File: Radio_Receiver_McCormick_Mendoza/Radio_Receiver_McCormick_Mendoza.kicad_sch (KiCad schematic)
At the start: 7 parts

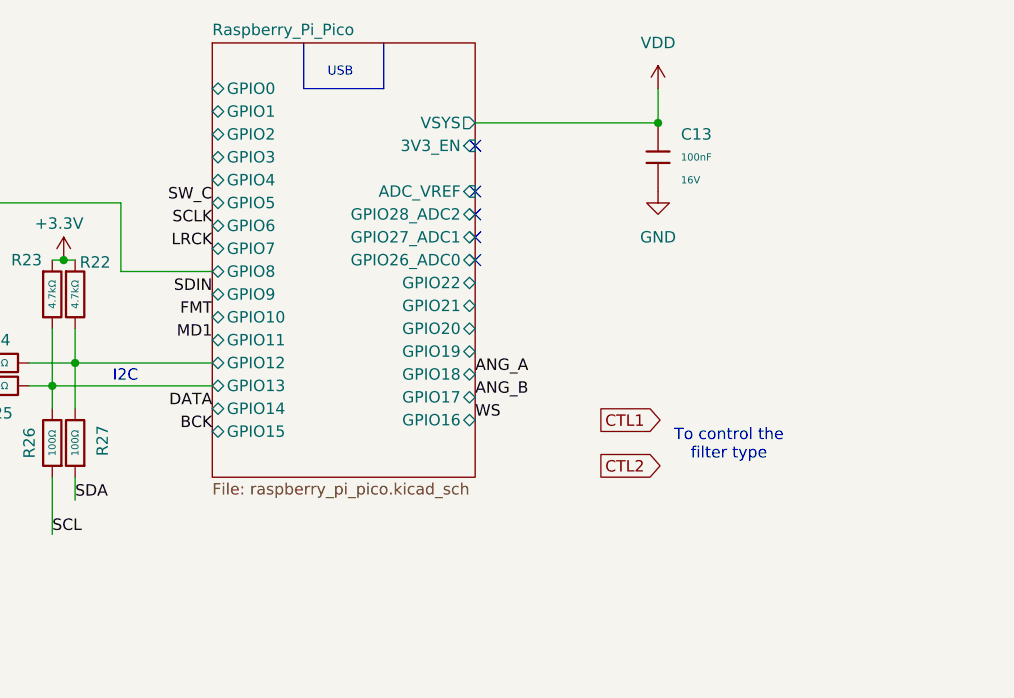
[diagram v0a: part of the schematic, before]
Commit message: Integrated signal path modules
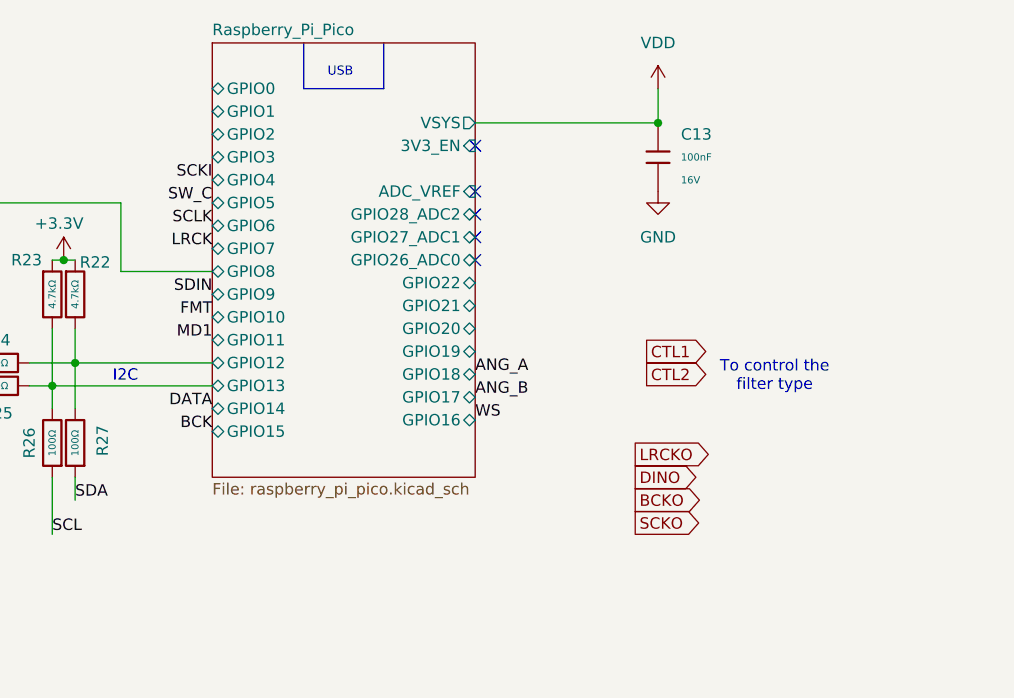
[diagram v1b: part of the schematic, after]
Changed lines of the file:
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@@
 	(text "To control the\nfilter type"
 		(exclude_from_sim no)
-		(at 128.524 80.264 0)
+		(at 133.604 72.644 0)
 		(effects
 			(font
@@
 		)
 	)
+	(label "SCKI"
+		(at 71.12 50.8 180)
+		(effects
+			(font
+				(size 1.27 1.27)
+			)
+			(justify right bottom)
+		)
+	)
 	(label "OSC_SCL"
 		(at 39.37 73.66 180)
@@
 	(global_label "CTL1"
 		(shape output)
-		(at 114.3 77.47 0)
+		(at 119.38 69.85 0)
+		(fields_autoplaced yes)
+		(effects
+			(font
+				(size 1.27 1.27)
+			)
+			(justify left)
+		)
+		(property "Intersheetrefs" "${INTERSHEET_REFS}"
+			(at 126.8404 69.85 0)
+			(hide yes)
+			(show_name no)
+			(do_not_autoplace no)
+			(effects
+				(font
+					(size 1.27 1.27)
+				)
+				(justify left)
+			)
+		)
+	)
+	(global_label "SCKO"
+		(shape output)
+		(at 118.11 88.9 0)
 		(fields_autoplaced yes)
 		(effects
@@
 		)
 		(property "Intersheetrefs" "${INTERSHEET_REFS}"
-			(at 121.7604 77.47 0)
+			(at 126.1752 88.9 0)
+			(hide yes)
+			(show_name no)
+			(do_not_autoplace no)
+			(effects
+				(font
+					(size 1.27 1.27)
+				)
+				(justify left)
+			)
+		)
+	)
+	(global_label "LRCKO"
+		(shape output)
+		(at 118.11 81.28 0)
+		(fields_autoplaced yes)
+		(effects
+			(font
+				(size 1.27 1.27)
+			)
+			(justify left)
+		)
+		(property "Intersheetrefs" "${INTERSHEET_REFS}"
+			(at 127.2638 81.28 0)
+			(hide yes)
+			(show_name no)
+			(do_not_autoplace no)
+			(effects
+				(font
+					(size 1.27 1.27)
+				)
+				(justify left)
+			)
+		)
+	)
+	(global_label "DINO"
+		(shape output)
+		(at 118.11 83.82 0)
+		(fields_autoplaced yes)
+		(effects
+			(font
+				(size 1.27 1.27)
+			)
+			(justify left)
+		)
+		(property "Intersheetrefs" "${INTERSHEET_REFS}"
+			(at 125.631 83.82 0)
 			(hide yes)
 			(show_name no)
@@
 	(global_label "CTL2"
 		(shape output)
-		(at 114.3 82.55 0)
+		(at 119.38 72.39 0)
+		(fields_autoplaced yes)
+		(effects
+			(font
+				(size 1.27 1.27)
+			)
+			(justify left)
+		)
+		(property "Intersheetrefs" "${INTERSHEET_REFS}"
+			(at 126.8404 72.39 0)
+			(hide yes)
+			(show_name no)
+			(do_not_autoplace no)
+			(effects
+				(font
+					(size 1.27 1.27)
+				)
+				(justify left)
+			)
+		)
+	)
+	(global_label "BCKO"
+		(shape output)
+		(at 118.11 86.36 0)
 		(fields_autoplaced yes)
 		(effects
@@
 		)
 		(property "Intersheetrefs" "${INTERSHEET_REFS}"
-			(at 121.7604 82.55 0)
+			(at 126.2357 86.36 0)
 			(hide yes)
 			(show_name no)

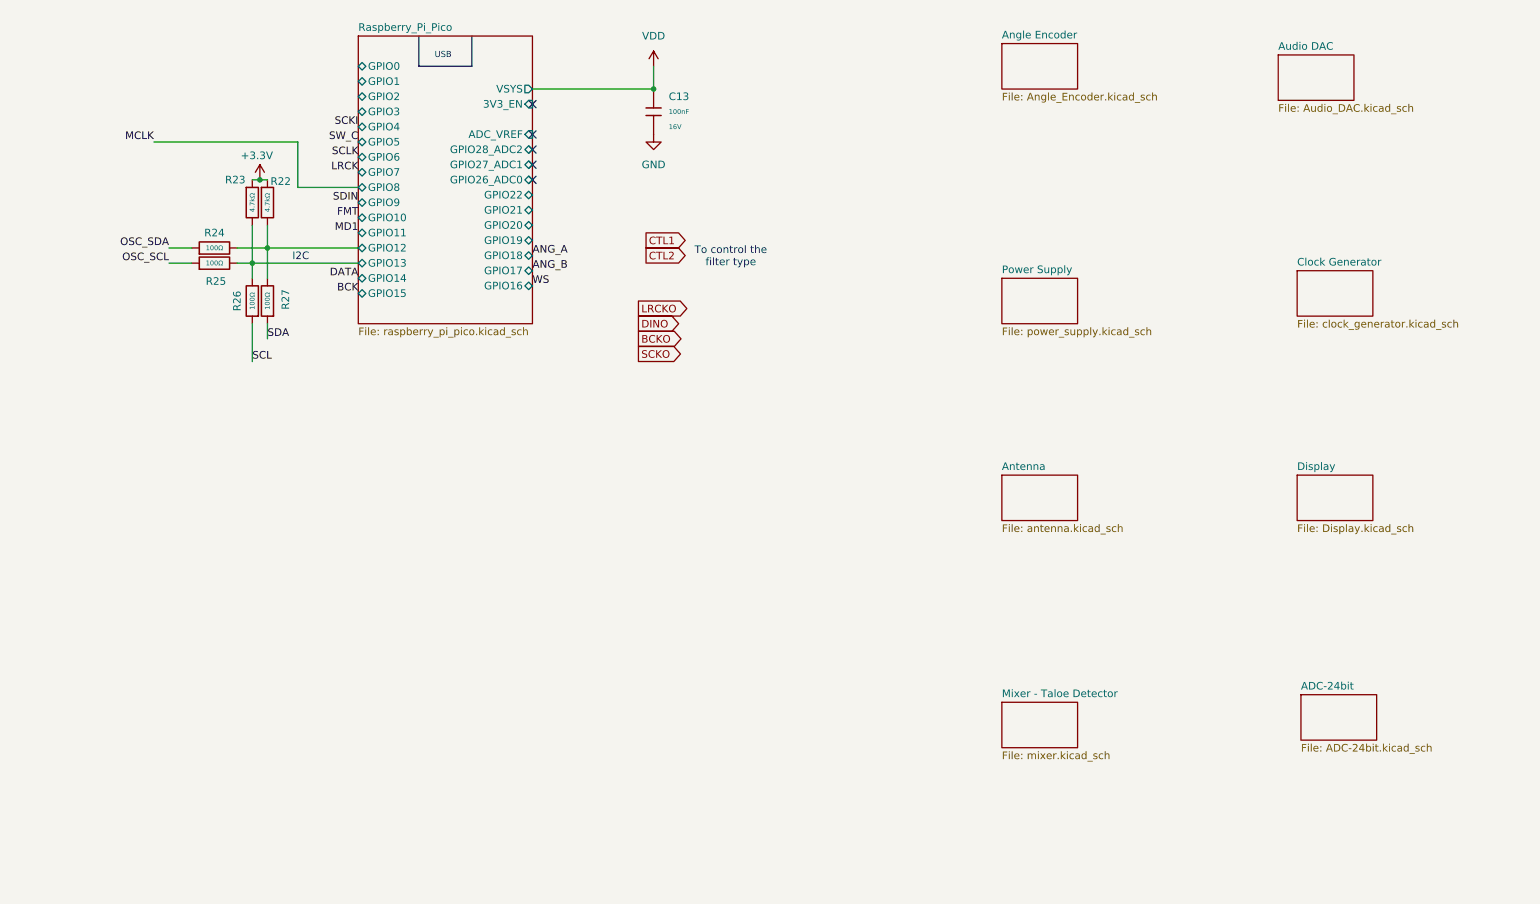
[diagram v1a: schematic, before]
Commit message: Finalized Pico connections and added indicator LEDs
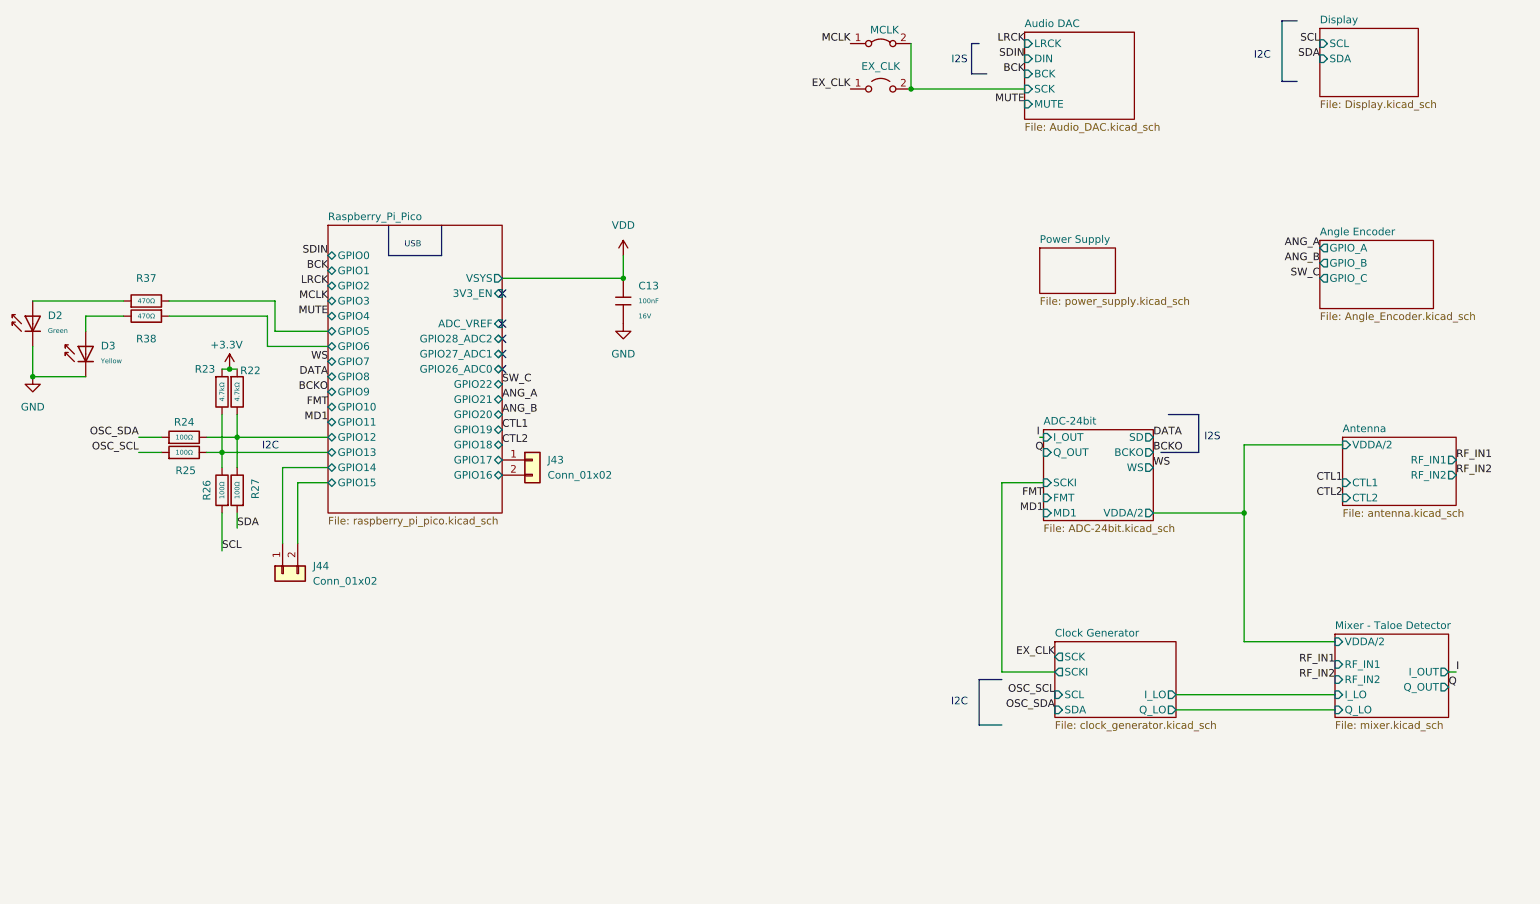
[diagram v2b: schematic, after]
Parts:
- added D2: Green, PCM_JLCPCB:D_0805, symbol PCM_JLCPCB-Diodes:LED,0805,Green
- added D3: Yellow, PCM_JLCPCB:D_0805, symbol PCM_JLCPCB-Diodes:LED,0805,Yellow
- added J43, J44: Conn_01x02, Connector_PinHeader_2.54mm:PinHeader_1x02_P2.54mm_Vertical, symbol Connector_Generic:Conn_01x02
- added JP13: EX_CLK, Jumper:SolderJumper-2_P1.3mm_Open_RoundedPad1.0x1.5mm, symbol Jumper:Jumper_2_Open
- added R37, R38: 470Ω, PCM_JLCPCB:R_0603, symbol PCM_JLCPCB-Resistors:0603,470Ω
- added e9: MCLK, Jumper:SolderJumper-2_P1.3mm_Bridged_RoundedPad1.0x1.5mm, symbol Jumper:Jumper_2_Bridged
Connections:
- net GND: now also D2.1, D3.1
- net MCLK: now also e9.1 (A)
- new net: D2.2, R37.1
- new net: D3.2, R38.2
- new net Audio DAC/SCK: JP13.2 (B), e9.2 (B)
- new net EX_CLK: JP13.1 (A)
- new net Raspberry_Pi_Pico/GPIO14: J44.1 (Pin_1)
- new net Raspberry_Pi_Pico/GPIO15: J44.2 (Pin_2)
- new net Raspberry_Pi_Pico/GPIO16: J43.2 (Pin_2)
- new net Raspberry_Pi_Pico/GPIO17: J43.1 (Pin_1)
- new net Raspberry_Pi_Pico/GPIO5: R37.2
- new net Raspberry_Pi_Pico/GPIO6: R38.1
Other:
- sheet ADC-24bit ports: added BCKO, FMT, I_OUT, MD1, Q_OUT, SCKI, SD, VDDA/2, WS; removed none
- sheet Angle Encoder ports: added GPIO_A, GPIO_B, GPIO_C; removed none
- sheet Antenna ports: added CTL1, CTL2, RF_IN1, RF_IN2, VDDA/2; removed none
- sheet Audio DAC ports: added BCK, DIN, LRCK, MUTE, SCK; removed none
- sheet Clock Generator ports: added I_LO, Q_LO, SCK, SCKI, SCL, SDA; removed none
- sheet Display ports: added SCL, SDA; removed none
- sheet Mixer - Taloe Detector ports: added I_LO, I_OUT, Q_LO, Q_OUT, RF_IN1, RF_IN2, VDDA/2; removed none
- note added: "I2S"
- note removed: "To control the filter type"
- moved on the sheet: C13, R22, R23, R24, R25, R26, R27

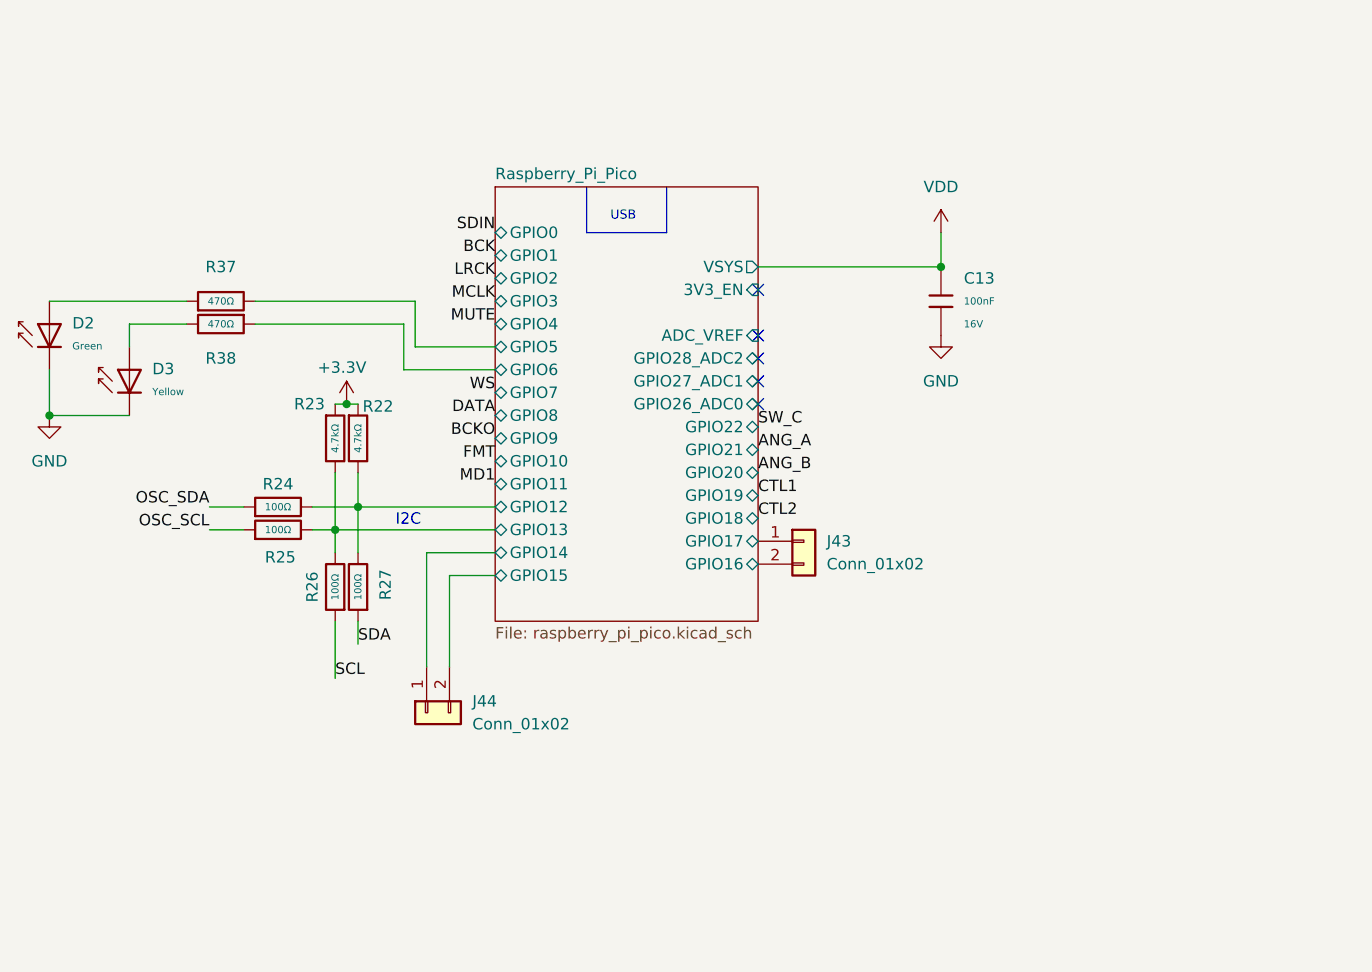
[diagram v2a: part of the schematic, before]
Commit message: Added transformer footprint and datasheet
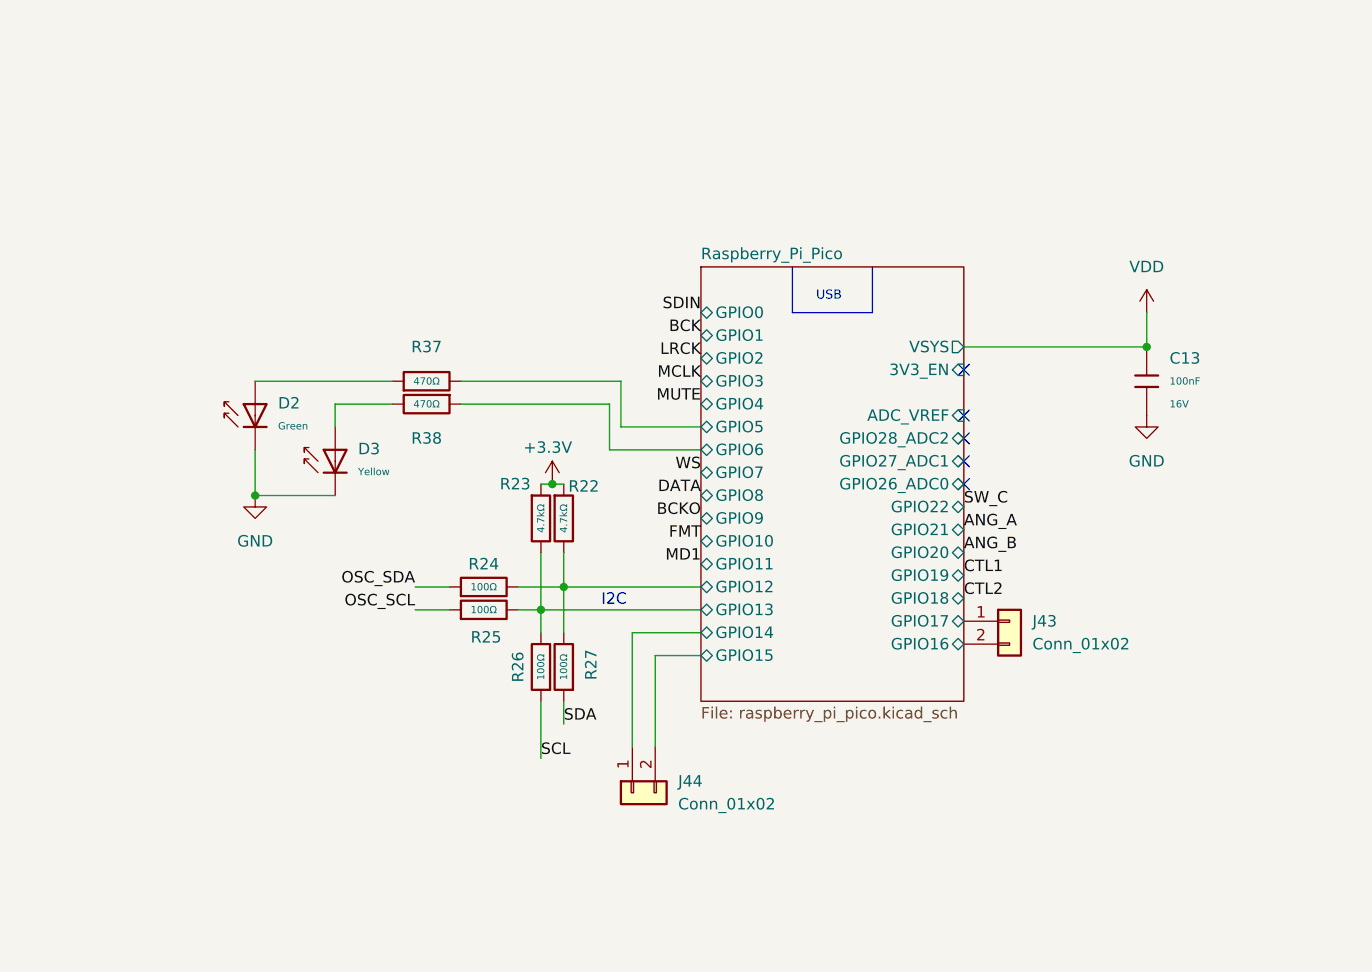
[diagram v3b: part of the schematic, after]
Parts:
- D2, D3: Manufacturer Hubei KENTO Elec -> (none)
- R37, R38: Manufacturer UNI-ROYAL(Uniroyal Elec) -> (none)
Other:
- moved on the sheet: C13, D2, D3, J43, J44, R22, R23, R24, R25, R26, R27, R37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

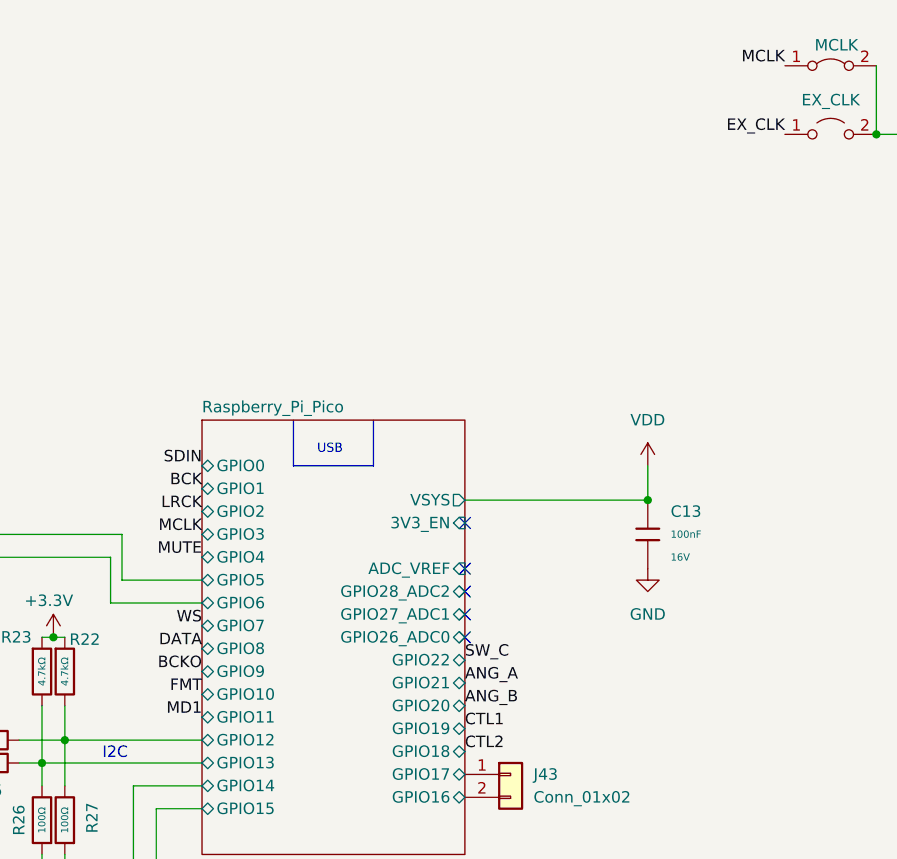
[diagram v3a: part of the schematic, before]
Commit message: Swapped voltage regulator to output 4.5V
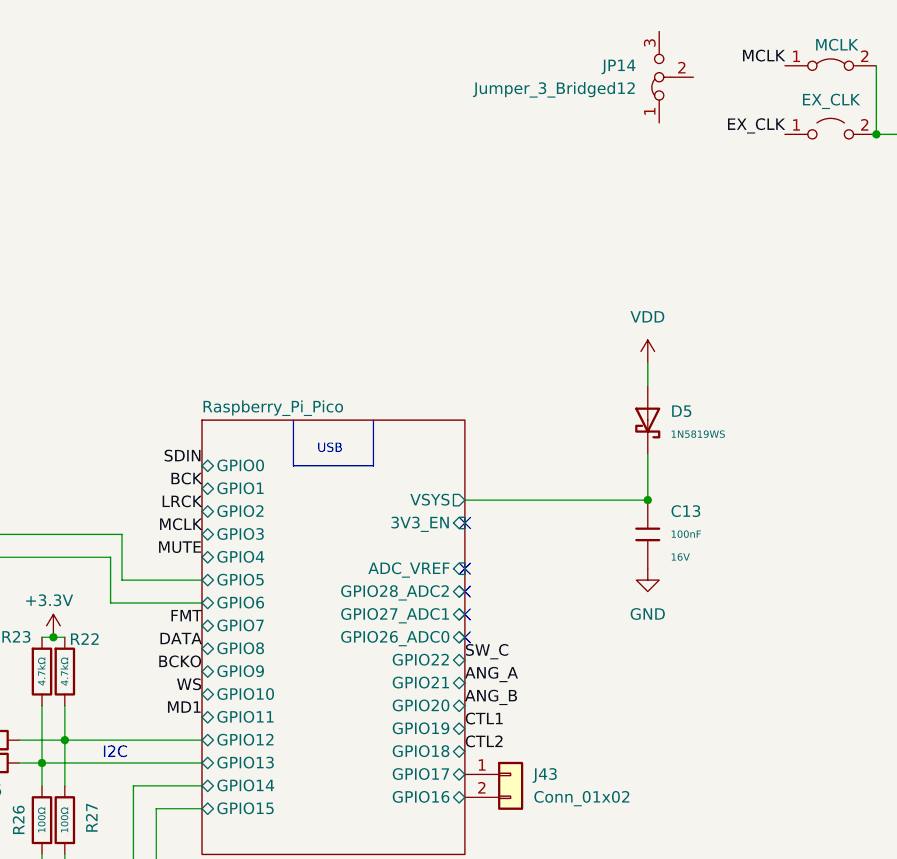
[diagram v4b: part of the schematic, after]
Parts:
- added D5: 1N5819WS, PCM_JLCPCB:D_SOD-323, symbol PCM_JLCPCB-Diodes:Schottky,1N5819WS
- added JP14: Jumper_3_Bridged12, symbol Jumper:Jumper_3_Bridged12
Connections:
- net VDD: now also D5.2; no longer C13.1
- new net Raspberry_Pi_Pico/VSYS: C13.1, D5.1
